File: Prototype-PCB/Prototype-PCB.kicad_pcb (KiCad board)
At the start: 2 copper layers, 89.4 x 12.6 mm, 11 parts, among them SW1 SW_SPST, SW2 SW_SPST, SW3 SW_SPST, SW4 SW_SPST

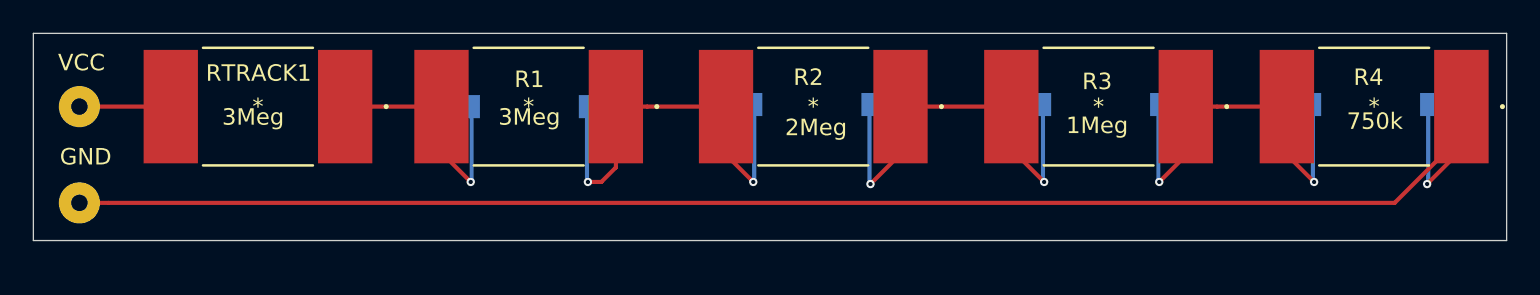
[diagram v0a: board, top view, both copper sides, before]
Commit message: Modified the pcb file. Changed the footprints for SMT resistors.
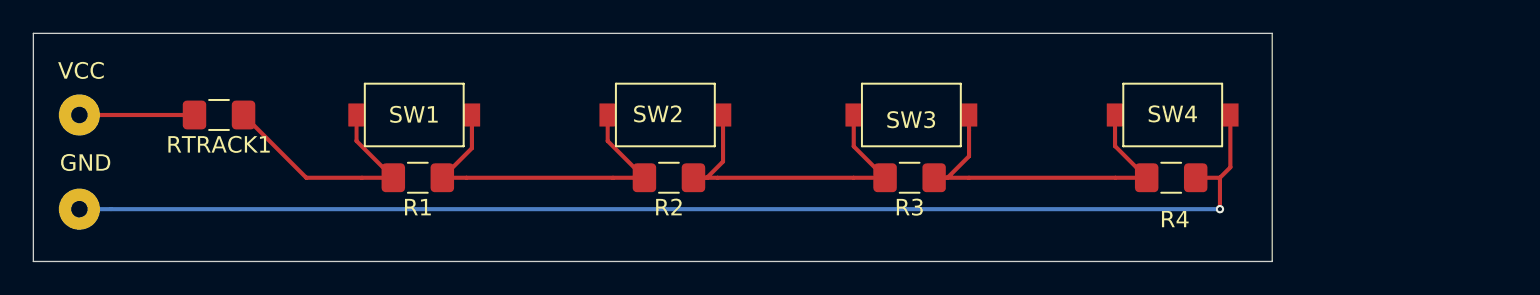
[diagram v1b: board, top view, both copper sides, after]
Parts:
- R1: value 3Meg -> 9k; footprint 3Meg SMT Resistor:KTR18EZPF3004 -> Read-Rope:R_1206_3216Metric_Pad1.42x1.75mm_HandSolder
- R2: value 2Meg -> 7k; footprint 2Meg SMT Resistor:KTR18EZPF2004 -> Read-Rope:R_1206_3216Metric_Pad1.42x1.75mm_HandSolder
- R3: value 1Meg -> 3k; footprint 1Meg SMT Resistor:KTR18EZPF1004 -> Read-Rope:R_1206_3216Metric_Pad1.42x1.75mm_HandSolder
- R4: value 750k -> 1k; footprint 750k SMT Resistor:KTR18EZPF7503 -> Read-Rope:R_1206_3216Metric_Pad1.42x1.75mm_HandSolder
- RTRACK1: value 3Meg -> 20k; footprint 3Meg SMT Resistor:KTR18EZPF3004 -> Read-Rope:R_1206_3216Metric_Pad1.42x1.75mm_HandSolder
- SW1, SW2, SW3, SW4: footprint KSR221GNCLFS-SMT:KSR221GNCLFS-SMT-NCSPST -> Read-Rope:KSR221GNCLFS-SMT-NCSPST; moved to F.Cu
- moved R4 13.1 mm to (161.5, 104.1)
- moved R3 12.3 mm to (145.6, 104.1)
- moved SW4 12.0 mm to (161.6, 100.3)
- moved SW3 11.5 mm to (145.7, 100.3)
- moved R2 9.77 mm to (131.0, 104.1)
- moved SW2 8.91 mm to (130.8, 100.3)
- moved R1 7.99 mm to (115.8, 104.1)
- moved SW1 7.00 mm to (115.6, 100.3)
- moved RTRACK1 2.42 mm to (103.7, 100.3)
- moved VCC 0.51 mm to (95.2, 100.3)
- moved GND 0.38 mm to (95.2, 106.0)
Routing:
- net GND: track 97.8 -> 76.7 mm
- net Net-(R2-Pad1): track 27.2 -> 21.3 mm, vias 2 -> 0
- net Net-(R1-Pad1): track 27.0 -> 21.6 mm, vias 2 -> 0
- net Net-(R3-Pad1): track 26.1 -> 22.7 mm, vias 2 -> 0
- net vout: track 17.8 -> 15.4 mm, vias 1 -> 0
- net VCC: track 5.54 -> 6.98 mm
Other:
- board size 89.4 x 12.6 mm -> 75.2 x 13.8 mm

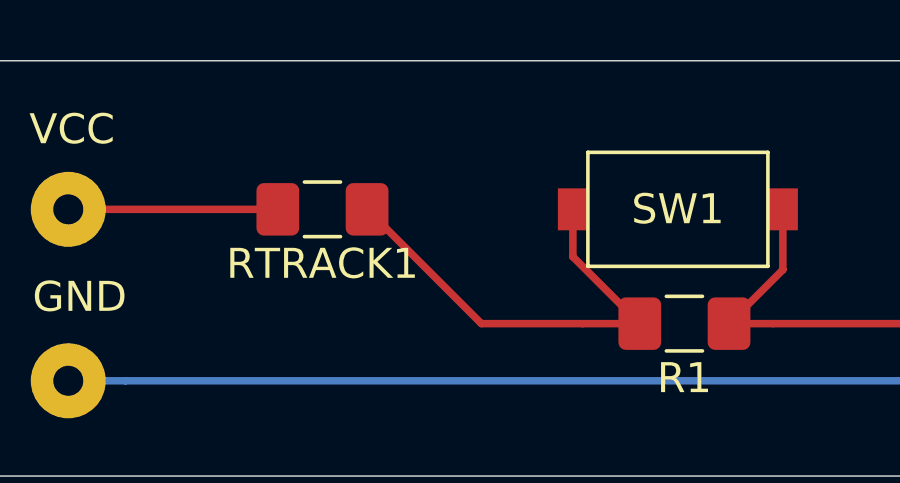
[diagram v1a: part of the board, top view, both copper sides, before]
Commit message: Fixed a mistake. Added a through-hole pad to connect output.
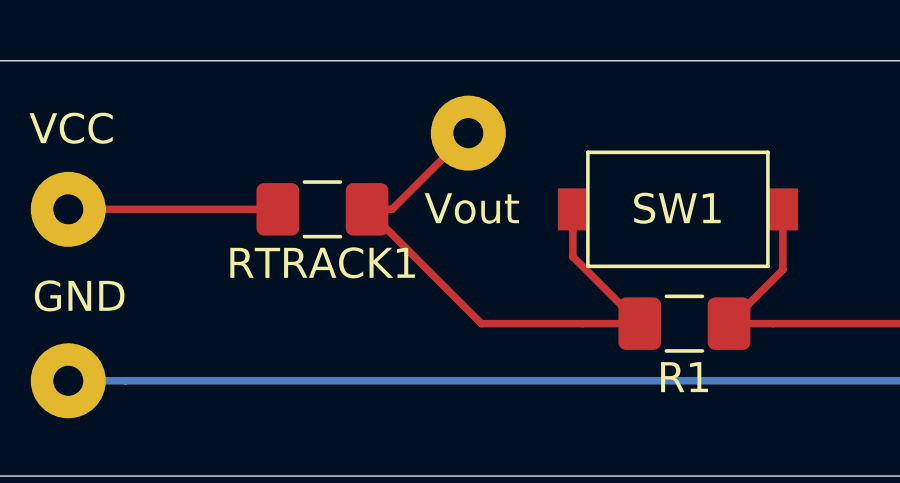
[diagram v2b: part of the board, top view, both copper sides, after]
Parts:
- added Vout: SolderWirePad_1x01_Drill1mm, Connector_Wire:SolderWirePad_1x01_Drill1mm, F.Cu at (108.6, 97.8)
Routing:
- net vout: track 15.4 -> 19.8 mm
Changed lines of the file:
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@@
     (thickness 1.6)
     (drawings 4)
-    (tracks 39)
+    (tracks 41)
     (zones 0)
-    (modules 11)
+    (modules 12)
     (nets 7)
   )
@@
   )
   (module Connector_Wire:SolderWirePad_1x01_Drill1mm (layer F.Cu)
+    (at 108.585 97.79)
+    (descr "Wire solder connection")
+    (tags connector)
+    (attr virtual)
+    (fp_text reference Vout (at 0.127 2.54) (layer F.SilkS)
+      (effects (font (size 1 1) (thickness 0.15)))
+    )
+    (fp_text value SolderWirePad_1x01_Drill1mm (at 0 3.175) (layer F.Fab)
+      (effects (font (size 1 1) (thickness 0.15)))
+    )
+    (fp_text user %R (at 0 0) (layer F.Fab)
+      (effects (font (size 1 1) (thickness 0.15)))
+    )
+    (fp_line (start -1.75 -1.75) (end 1.75 -1.75) (layer F.CrtYd) (width 0.05))
+    (fp_line (start -1.75 -1.75) (end -1.75 1.75) (layer F.CrtYd) (width 0.05))
+    (fp_line (start 1.75 1.75) (end 1.75 -1.75) (layer F.CrtYd) (width 0.05))
+    (fp_line (start 1.75 1.75) (end -1.75 1.75) (layer F.CrtYd) (width 0.05))
+    (pad 1 thru_hole circle (at 0 0) (size 2.49936 2.49936) (drill 1.00076) (layers *.Cu *.Mask)
+      (net 1 vout))
+  )
+  (module Connector_Wire:SolderWirePad_1x01_Drill1mm (layer F.Cu)
     (at 95.25 106.045)
     (descr "Wire solder connection")
@@
   (segment (start 112.07 101.91) (end 114.3 104.14) (width 0.25) (layer F.Cu) (net 1))
   (segment (start 112.07 100.33) (end 112.07 101.91) (width 0.25) (layer F.Cu) (net 1))
+  (segment (start 106.045 100.33) (end 108.585 97.79) (width 0.25) (layer F.Cu) (net 1))
+  (segment (start 105.21 100.33) (end 106.045 100.33) (width 0.25) (layer F.Cu) (net 1))
   (segment (start 118.745 104.14) (end 117.275 104.14) (width 0.25) (layer F.Cu) (net 2))
   (segment (start 129.54 104.14) (end 127.635 104.14) (width 0.25) (layer F.Cu) (net 2))
